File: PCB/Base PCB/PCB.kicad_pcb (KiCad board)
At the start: 2 copper layers, 66 x 66 mm, 12 parts, among them J1 Conn_01x19_Socket, J2 Conn_01x19_Socket, J3 Conn_01x03_Socket, J4 Conn_01x09_Socket, J5 Conn_01x01_Socket, J6 Conn_01x01_Socket, J7 Conn_01x01_Socket, J8 Conn_01x01_Socket

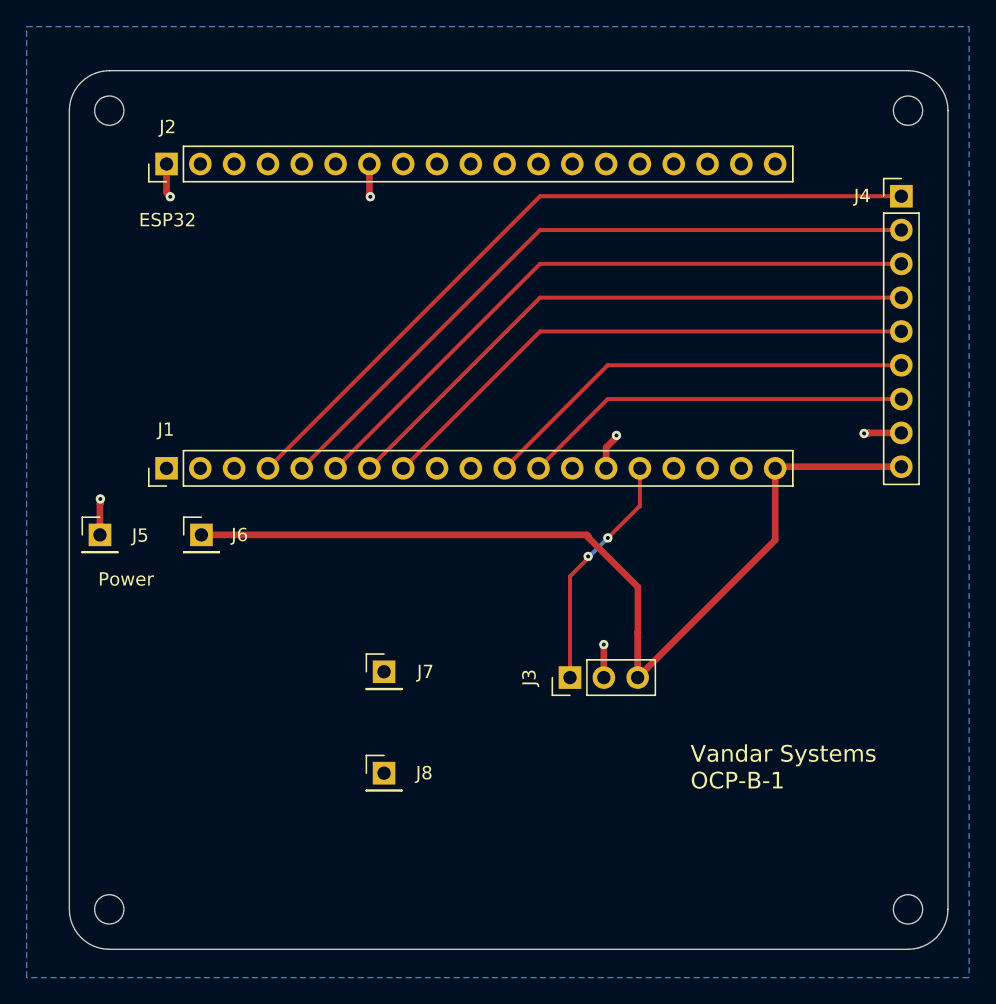
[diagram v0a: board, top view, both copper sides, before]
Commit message: Finished the rough draft for the enclosure. I used the 3d models from KiCad to get the PCB dimensions.
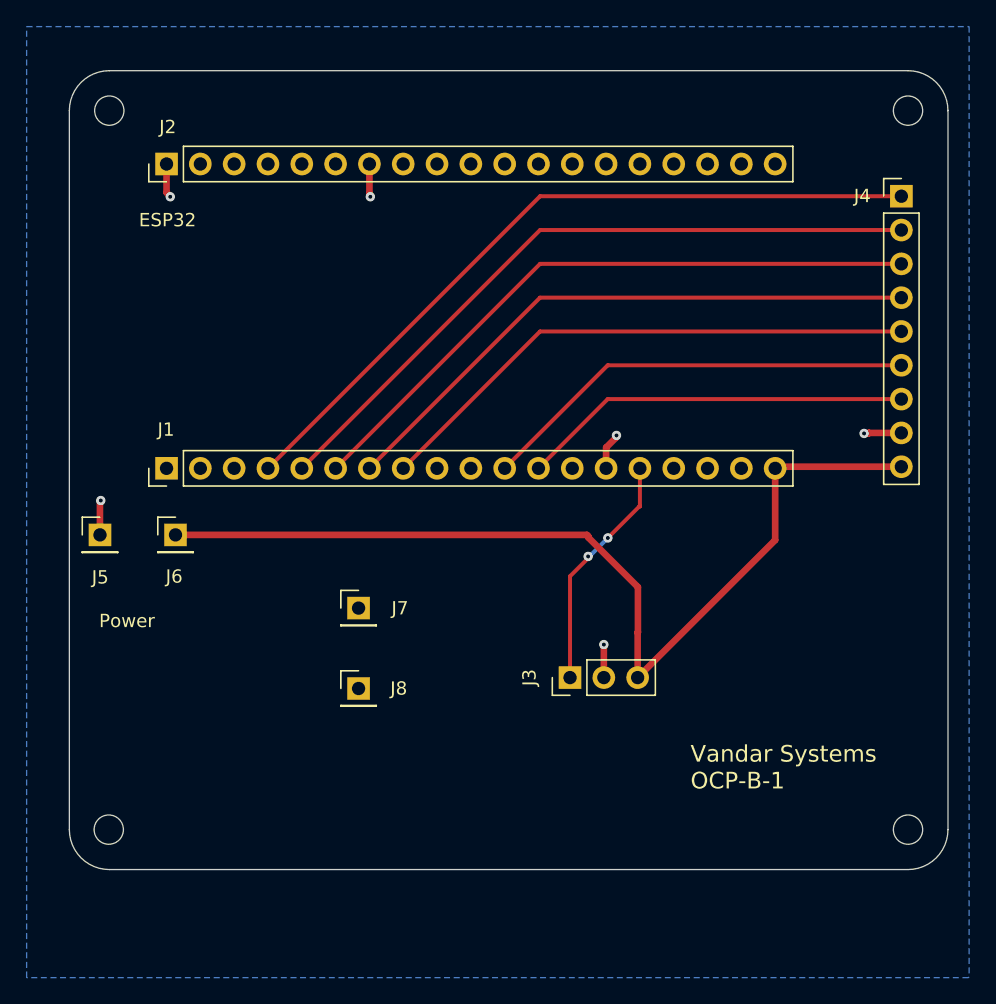
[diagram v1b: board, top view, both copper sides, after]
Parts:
- moved J8 6.64 mm to (94.4, 119.4)
- moved H2 5.99 mm to (75.7, 130.0)
- moved H2 5.99 mm to (135.7, 130.0)
- moved J7 5.15 mm to (94.4, 113.4)
- moved J6 1.95 mm to (80.7, 107.9)
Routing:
- net 5V: track 70.8 -> 72.7 mm
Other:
- board size 66 x 66 mm -> 66 x 60 mm
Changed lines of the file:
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@@
 			(usegerberattributes yes)
 			(usegerberadvancedattributes yes)
-			(creategerberjobfile no)
+			(creategerberjobfile yes)
 			(dashed_line_dash_ratio 12.000000)
 			(dashed_line_gap_ratio 3.000000)
@@
 		)
 		(fp_text user "${REFERENCE}"
-			(at 0 22.86 360)
+			(at 0 22.86 0)
 			(layer "F.Fab")
 			(effects
@@
 	(footprint "Connector_PinHeader_2.54mm:PinHeader_1x01_P2.54mm_Vertical"
 		(layer "F.Cu")
-		(at 82.62 107.86)
+		(at 80.675 107.86)
 		(descr "Through hole straight pin header, 1x01, 2.54mm pitch, single row")
 		(tags "Through hole pin header THT 1x01 2.54mm single row")
 		(property "Reference" "J6"
-			(at 2.88 0.01 0)
+			(at -0.1 3.13 0)
 			(layer "F.SilkS")
 			(effects
@@
 		)
 		(fp_text user "${REFERENCE}"
-			(at 0 22.86 360)
+			(at 0 22.86 0)
 			(layer "F.Fab")
 			(effects
@@
 	(footprint "MountingHole:MountingHole_2.2mm_M2"
 		(layer "F.Cu")
-		(at 135.7 135.99)
+		(at 135.7 130)
 		(descr "Mounting Hole 2.2mm, no annular, M2")
 		(tags "mounting hole 2.2mm no annular m2")
@@
 	(footprint "MountingHole:MountingHole_2.2mm_M2"
 		(layer "F.Cu")
-		(at 75.7 135.99)
+		(at 75.66 130)
 		(descr "Mounting Hole 2.2mm, no annular, M2")
 		(tags "mounting hole 2.2mm no annular m2")
@@
 		)
 		(fp_text user "${REFERENCE}"
-			(at 0 2.54 360)
+			(at 0 2.54 0)
 			(layer "F.Fab")
 			(effects
@@
 		(tags "Through hole pin header THT 1x01 2.54mm single row")
 		(property "Reference" "J5"
-			(at 3.03 0.05 0)
+			(at 0.02 3.19 0)
 			(layer "F.SilkS")
 			(effects
@@
 	(footprint "Connector_PinHeader_2.54mm:PinHeader_1x01_P2.54mm_Vertical"
 		(layer "F.Cu")
-		(at 96.34 118.14)
+		(at 94.425 113.36)
 		(descr "Through hole straight pin header, 1x01, 2.54mm pitch, single row")
 		(tags "Through hole pin header THT 1x01 2.54mm single row")
@@
 	(footprint "Connector_PinHeader_2.54mm:PinHeader_1x01_P2.54mm_Vertical"
 		(layer "F.Cu")
-		(at 96.34 125.76)
+		(at 94.425 119.4)
 		(descr "Through hole straight pin header, 1x01, 2.54mm pitch, single row")
 		(tags "Through hole pin header THT 1x01 2.54mm single row")
@@
 	)
 	(gr_line
-		(start 138.7 75.99)
-		(end 138.7 135.99)
+		(start 138.7 130)
+		(end 138.7 75.99)
 		(stroke
 			(width 0.05)
@@
 	)
 	(gr_line
-		(start 135.7 138.99)
-		(end 75.7 138.99)
+		(start 135.7 133)
+		(end 75.7 133)
 		(stroke
 			(width 0.05)
@@
 		(layer "Edge.Cuts")
 	)
-	(gr_arc
-		(start 75.7 138.99)
-		(mid 73.57868 138.11132)
-		(end 72.7 135.99)
+	(gr_line
+		(start 72.7 130)
+		(end 72.7 75.99)
 		(stroke
 			(width 0.05)
@@
 	)
 	(gr_arc
-		(start 138.7 135.99)
-		(mid 137.82132 138.11132)
-		(end 135.7 138.99)
+		(start 72.7 75.99)
+		(mid 73.57868 73.86868)
+		(end 75.7 72.99)
 		(stroke
 			(width 0.05)
@@
 	)
 	(gr_arc
-		(start 72.7 75.99)
-		(mid 73.57868 73.86868)
-		(end 75.7 72.99)
+		(start 75.7 133)
+		(mid 73.57868 132.12132)
+		(end 72.7 130)
 		(stroke
 			(width 0.05)
@@
 		(layer "Edge.Cuts")
 	)
-	(gr_line
-		(start 72.7 135.99)
-		(end 72.7 75.99)
+	(gr_arc
+		(start 138.7 130)
+		(mid 137.82132 132.12132)
+		(end 135.7 133)
 		(stroke
 			(width 0.05)
@@
 	)
 	(gr_text "Power"
-		(at 74.86 111.79 0)
+		(at 74.93 114.91 0)
 		(layer "F.SilkS")
 		(effects
@@
 	)
 	(segment
-		(start 75 105.52)
-		(end 75.03 105.49)
-		(width 0.5)
-		(layer "F.Cu")
-		(net 6)
-	)
-	(segment
 		(start 80 82.14)
 		(end 80.28 82.42)
@@
 	)
 	(segment
-		(start 132.72 100.24)
-		(end 132.4 100.24)
+		(start 75 107.86)
+		(end 75 105.34)
 		(width 0.5)
 		(layer "F.Cu")
@@
 	)
 	(segment
-		(start 95.24 82.39)
-		(end 95.31 82.46)
+		(start 132.72 100.24)
+		(end 132.4 100.24)
 		(width 0.5)
 		(layer "F.Cu")
@@
 	)
 	(segment
-		(start 75.03 105.49)
-		(end 75.03 105.16)
+		(start 95.24 82.39)
+		(end 95.31 82.46)
 		(width 0.5)
 		(layer "F.Cu")
@@
 	)
 	(segment
-		(start 75 107.86)
-		(end 75 105.52)
-		(width 0.5)
-		(layer "F.Cu")
-		(net 6)
-	)
-	(segment
 		(start 132.76 100.2)
 		(end 132.75 100.19)
@@
 	)
 	(segment
-		(start 75 105.52)
-		(end 75.01 105.51)
+		(start 75 105.34)
+		(end 75.06 105.28)
 		(width 0.5)
 		(layer "F.Cu")
@@
 	)
 	(via
-		(at 75.03 105.16)
+		(at 75.06 105.28)
 		(size 0.7)
 		(drill 0.3)
@@
 	)
 	(segment
-		(start 125.84 102.74)
-		(end 125.72 102.86)
+		(start 115.39 118.58)
+		(end 115.39 115.201472)
 		(width 0.5)
 		(layer "F.Cu")
@@
 	)
 	(segment
-		(start 111.68 107.96)
-		(end 111.58 107.86)
+		(start 125.84 102.74)
+		(end 125.72 102.86)
 		(width 0.5)
 		(layer "F.Cu")
@@
 	)
 	(segment
-		(start 115.41 115.181472)
-		(end 115.41 111.78)
+		(start 115.39 115.201472)
+		(end 115.41 115.181472)
 		(width 0.5)
 		(layer "F.Cu")
@@
 	)
 	(segment
-		(start 115.39 115.201472)
-		(end 115.41 115.181472)
+		(start 115.41 111.78)
+		(end 111.68 108.05)
 		(width 0.5)
 		(layer "F.Cu")
@@
 	)
 	(segment
-		(start 111.58 107.86)
-		(end 82.62 107.86)
+		(start 115.41 115.181472)
+		(end 115.41 111.78)
 		(width 0.5)
 		(layer "F.Cu")
@@
 	)
 	(segment
-		(start 115.41 111.78)
-		(end 111.68 108.05)
+		(start 111.68 107.96)
+		(end 111.58 107.86)
 		(width 0.5)
 		(layer "F.Cu")
@@
 	)
 	(segment
-		(start 115.39 118.58)
-		(end 115.39 115.201472)
+		(start 111.68 108.05)
+		(end 111.68 107.96)
 		(width 0.5)
 		(layer "F.Cu")
@@
 	)
 	(segment
-		(start 125.72 108.25)
-		(end 115.39 118.58)
+		(start 80.675 107.86)
+		(end 111.58 107.86)
 		(width 0.5)
 		(layer "F.Cu")
@@
 	)
 	(segment
-		(start 111.68 108.05)
-		(end 111.68 107.96)
+		(start 125.72 108.25)
+		(end 115.39 118.58)
 		(width 0.5)
 		(layer "F.Cu")
